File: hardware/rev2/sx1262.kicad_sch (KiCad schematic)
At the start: 36 parts, among them U2 SX1262IMLTRT, U3 PE4259, Y2 TCXO 32MHz

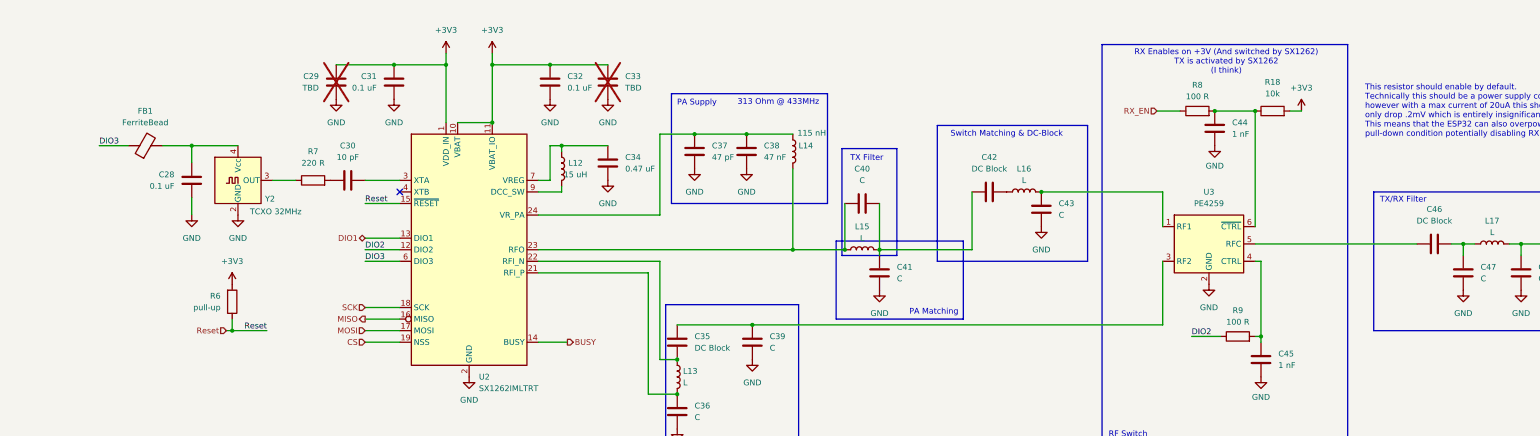
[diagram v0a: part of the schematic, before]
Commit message: set all applicable components for sx1262
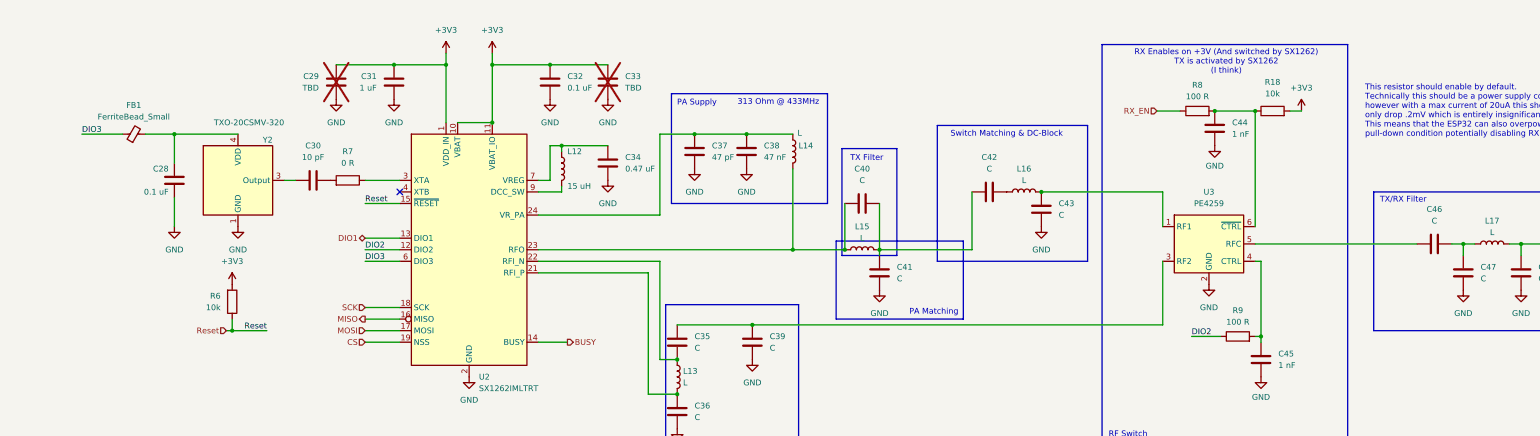
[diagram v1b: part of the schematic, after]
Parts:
- removed FB1: FerriteBead, symbol Device:FerriteBead
- removed Y2: TCXO 32MHz, symbol Oscillator:TCXO-14
- added FB1: FerriteBead_Small, Inductor_SMD:L_0402_1005Metric_Pad0.77x0.64mm_HandSolder, symbol Device:FerriteBead_Small
- added Y2: TXO-20CSMV-320, _footprints:TXO-20CSMV-320, symbol _symbols:TXO-20CSMV-320
- C28, C32: footprint Capacitor_SMD:C_0603_1608Metric_Pad1.08x0.95mm_HandSolder -> Capacitor_SMD:C_0402_1005Metric_Pad0.74x0.62mm_HandSolder; Mouser Part Number 81-GCJ188R71E104KA2D -> 81-GRM155R71H104KE4D
- C29, C33: footprint Capacitor_SMD:C_0603_1608Metric_Pad1.08x0.95mm_HandSolder -> Capacitor_SMD:C_0402_1005Metric_Pad0.74x0.62mm_HandSolder; now in the parts list
- C30: footprint Capacitor_SMD:C_0603_1608Metric_Pad1.08x0.95mm_HandSolder -> Capacitor_SMD:C_0402_1005Metric_Pad0.74x0.62mm_HandSolder; Mouser Part Number (none) -> 81-GJM1555C1H100JB01
- C31: value 0.1 uF -> 1 uF; footprint Capacitor_SMD:C_0603_1608Metric_Pad1.08x0.95mm_HandSolder -> Capacitor_SMD:C_0402_1005Metric_Pad0.74x0.62mm_HandSolder; Mouser Part Number 81-GCJ188R71E104KA2D -> 81-GRM155R61C105KA2D
- C34: footprint Capacitor_SMD:C_0603_1608Metric_Pad1.08x0.95mm_HandSolder -> Capacitor_SMD:C_0402_1005Metric_Pad0.74x0.62mm_HandSolder; Mouser Part Number (none) -> 81-GRM155R71A474KE1D
- C35, C42, C46: value DC Block -> C
- C37: Mouser Part Number (none) -> 81-GJM1555C1H470JB1D
- C38: Mouser Part Number (none) -> 81-GRM155R71C473KA01
- C44, C45: Mouser Part Number (none) -> 81-GRM155R72A102KA1D
- L12: Mouser Part Number (none) -> 810-MLZ1608N150LT000
- L14: value 115 nH -> L
- R18: footprint Inductor_SMD:L_0603_1608Metric_Pad1.05x0.95mm_HandSolder -> Resistor_SMD:R_0603_1608Metric_Pad0.98x0.95mm_HandSolder
- R6: value pull-up -> 10k; footprint Inductor_SMD:L_0603_1608Metric_Pad1.05x0.95mm_HandSolder -> Resistor_SMD:R_0603_1608Metric_Pad0.98x0.95mm_HandSolder
- R7: value 220 R -> 0 R; footprint Inductor_SMD:L_0603_1608Metric_Pad1.05x0.95mm_HandSolder -> Resistor_SMD:R_0402_1005Metric_Pad0.72x0.64mm_HandSolder; Mouser Part Number (none) -> 71-CRCW04020000Z0EDC
- R8, R9: footprint Inductor_SMD:L_0603_1608Metric_Pad1.05x0.95mm_HandSolder -> Resistor_SMD:R_0402_1005Metric_Pad0.72x0.64mm_HandSolder; Mouser Part Number (none) -> 71-CRCW0402-100
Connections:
- net DIO3: now also FB1.1
- net at U2.3 (XTA): now also R7.1; no longer C30.2
- net at C28.2: now also FB1.2, Y2.4 (VDD)
- net GND renamed 2
- net 2: now also Y2.1 (GND), Y2.GND (2)
- new net: C30.2, Y2.3 (Output)
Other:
- moved on the sheet: C28, C30, R7

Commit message: continued routing and layouting
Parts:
- renumbered C28 to C26, C30 to C27, C29 to C28, C31 to C29, C32 to C30, C33 to C31, C34 to C32, C35 to C33, C36 to C34, C37 to C35, C38 to C36, C39 to C37, C40 to C38, C41 to C39, C42 to C40, C43 to C41, C44 to C42, C45 to C43, C46 to C44, C47 to C45, C48 to C46, R6 to R17, R7 to R18, R8 to R19, R9 to R20, R18 to R21, U2 to U3, U3 to U4

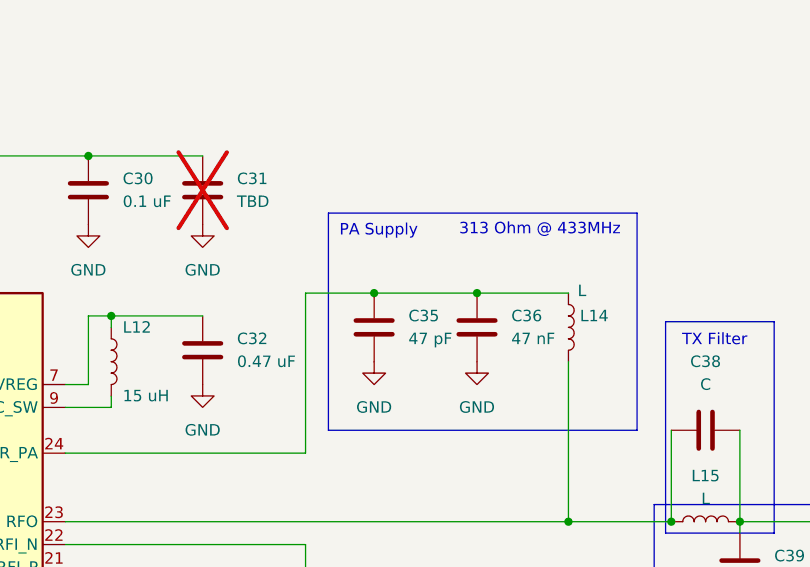
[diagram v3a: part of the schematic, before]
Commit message: continued layout, finished most of the RF stuff
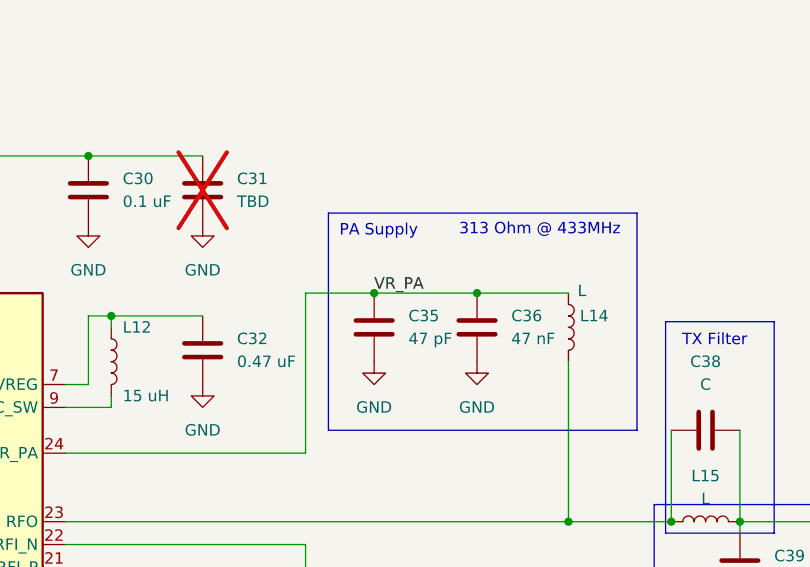
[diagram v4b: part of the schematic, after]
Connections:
- net VR_PA: now reaches C35.1, C36.1, L14.1, U3.24 (VR_PA)
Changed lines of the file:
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@@
+		)
+	)
+	(label "VR_PA"
+		(at 170.18 111.76 0)
+		(effects
+			(font
+				(size 1.27 1.27)
+			)
+			(justify left bottom)
 		)
 	)
@@
 		(length 1.27)
 		(shape round)
-		(at 181.61 111.76 0)
+		(at 238.76 124.46 0)
 		(fields_autoplaced yes)
 		(effects
@@
 			(justify left bottom)
 		)
-		(property "Net Class" "Power"
-			(at 182.3085 110.49 0)
+		(property "Net Class" "50 Ohm"
+			(at 239.4585 123.19 0)
 			(hide yes)
 			(show_name no)
@@
 		)
 		(property "Component Class" ""
-			(at -20.32 -24.13 0)
+			(at 69.85 -38.1 0)
 			(show_name no)
 			(do_not_autoplace no)

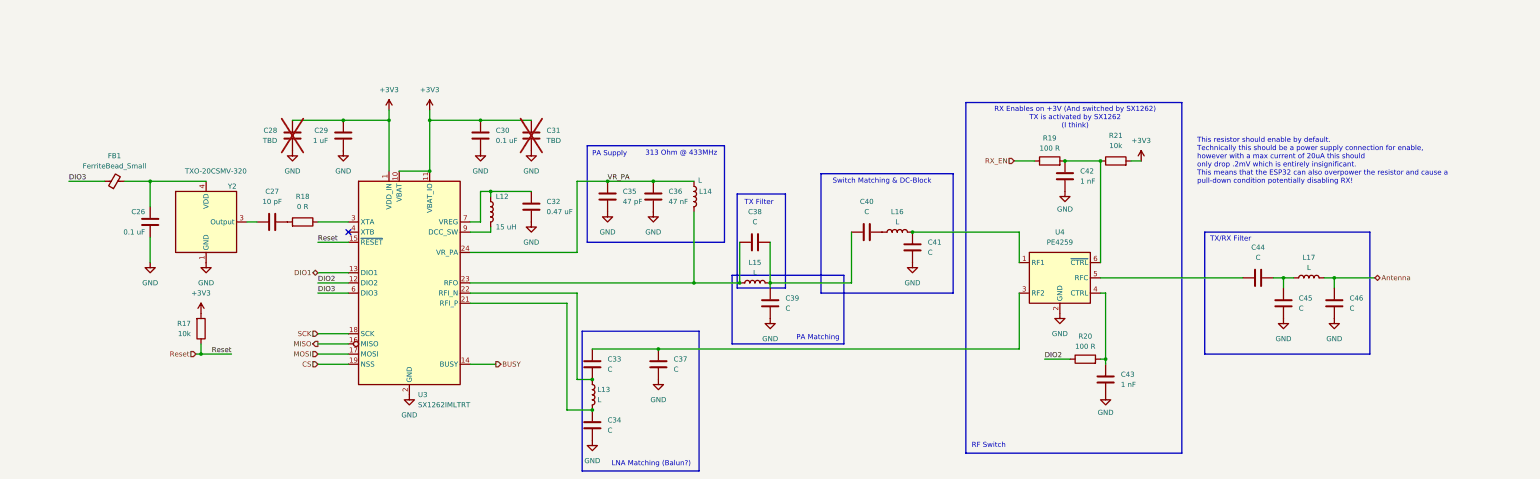
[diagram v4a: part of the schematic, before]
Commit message: finished routing most of the RF and power for SX1262 and ESP32, also decided final ish positions for both.
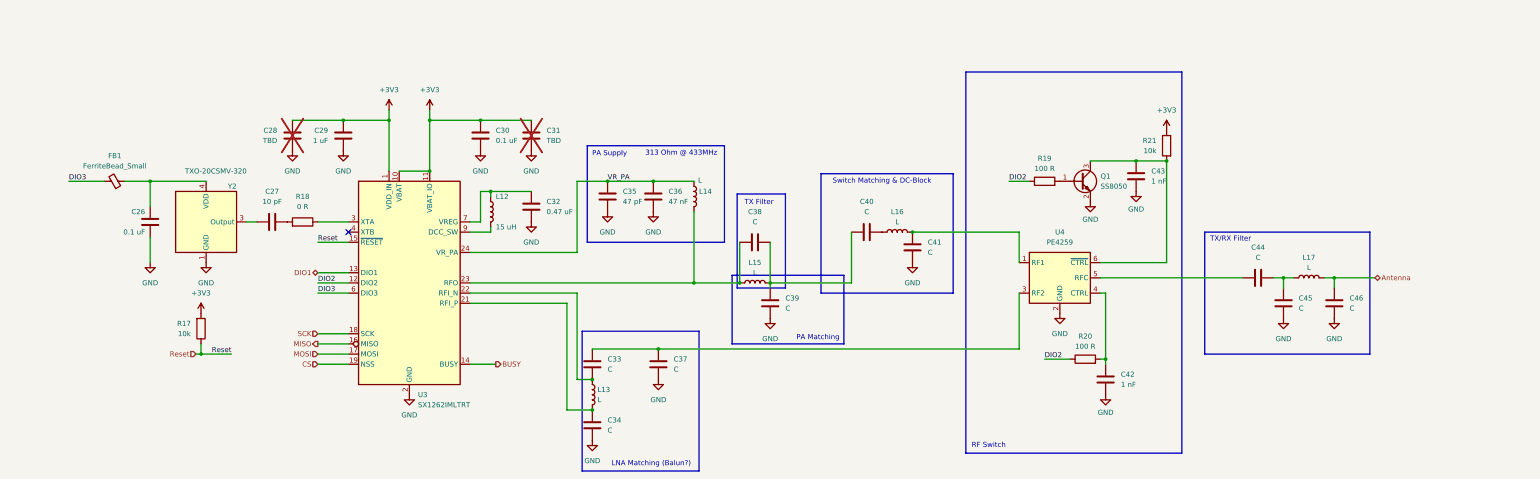
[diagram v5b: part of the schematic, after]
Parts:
- added Q1: SS8050, Package_TO_SOT_SMD:SOT-23, symbol Transistor_BJT:SS8050
- renumbered C43 to C42, C42 to C43
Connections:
- net RX_EN is gone; now on net DIO2: R19.1
- net +3V3: now also R21.1; no longer R21.2
- net DIO3: now also FB1.2; no longer FB1.1
- net at C43.1, U4.6 (~{CTRL}): now also R21.2, Q1.3 (C); no longer R19.2, R21.1
- net at C26.2, Y2.4 (VDD): now also FB1.1; no longer FB1.2
- net 2 renamed GND
- net GND: now also Y2.2 (GND), Q1.2 (E); no longer Y2.GND (2)
- new net: Q1.1 (B), R19.2
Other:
- note removed: "RX Enables on +3V (And switched by SX1262) TX is activated by SX1262 (I think)"
- note removed: "This resistor should enable by default. Technically this should be a power supply connection for enable, however with a max current of 20uA this should only drop .2mV which is entirely insignificant. This means that the ESP32 can also overpower the resistor and cause a pull-down condition potentially disabling RX!"
- moved on the sheet: C43, FB1, R19, R21

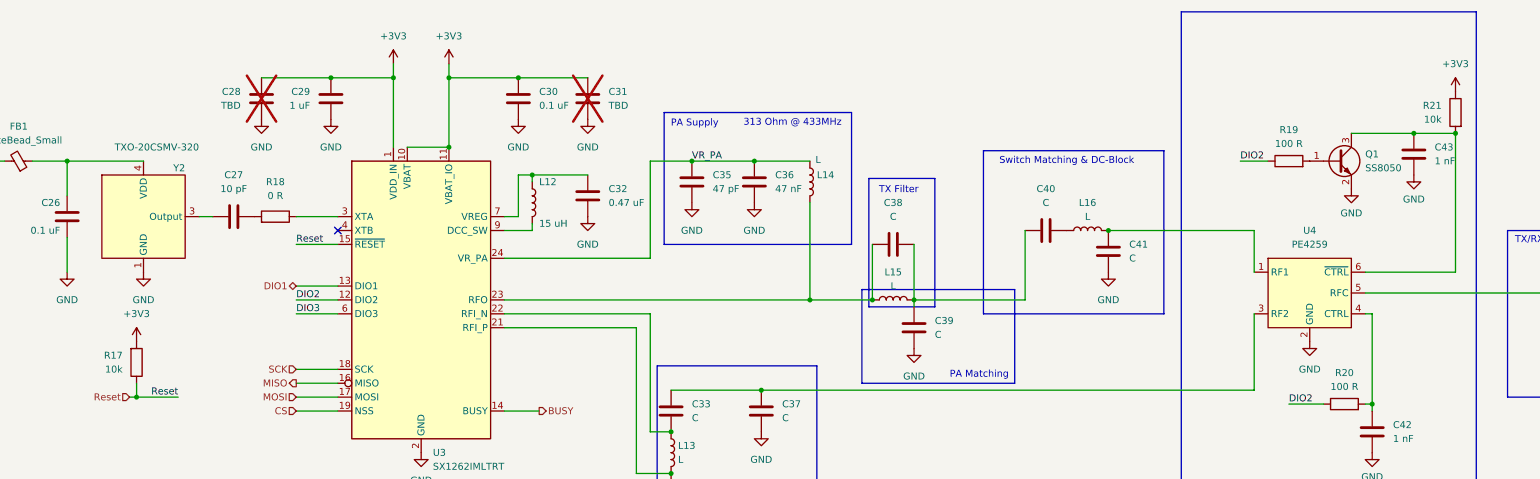
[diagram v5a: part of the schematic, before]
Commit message: routed everything ESP32 and SX1262, will hopefully work. still needs more testpoints
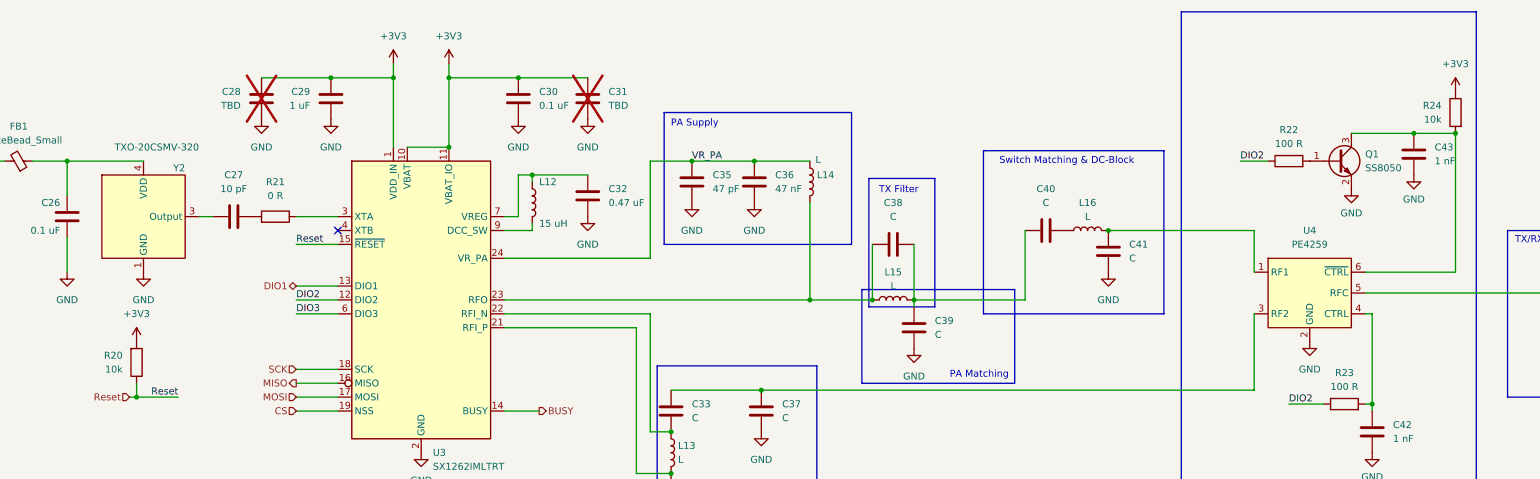
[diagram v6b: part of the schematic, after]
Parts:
- C26, C30: Mouser Part Number 81-GRM155R71H104KE4D -> 81-GRM155R71H104KE4D
- C29: Mouser Part Number 81-GRM155R61C105KA2D -> 81-GRM155R61C105KA2D
- C32: Mouser Part Number 81-GRM155R71A474KE1D -> 81-GRM155R71A474KE1D
- FB1: Mouser Part Number 81-BLM15PG100SN1D -> 81-BLM15PG100SN1D
- R21: renamed from R18; Mouser Part Number 71-CRCW04020000Z0EDC -> 71-CRCW04020000Z0EDC
- Y2: Mouser Part Number 520-TXO20CSMV320EYTR -> 520-TXO20CSMV320EYTR
- renumbered R17 to R20, R19 to R22, R20 to R23, R21 to R24
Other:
- note removed: "313 Ohm @ 433MHz"

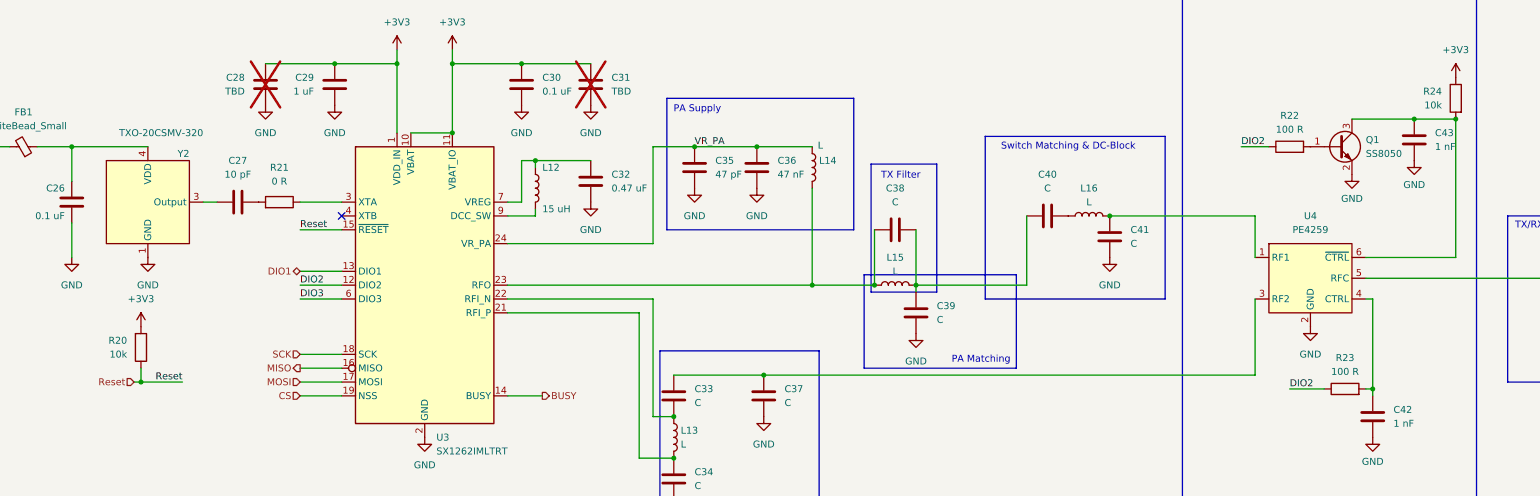
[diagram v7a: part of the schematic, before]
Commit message: added testpoints, added LEDs, fixed a lot of DRC stuff
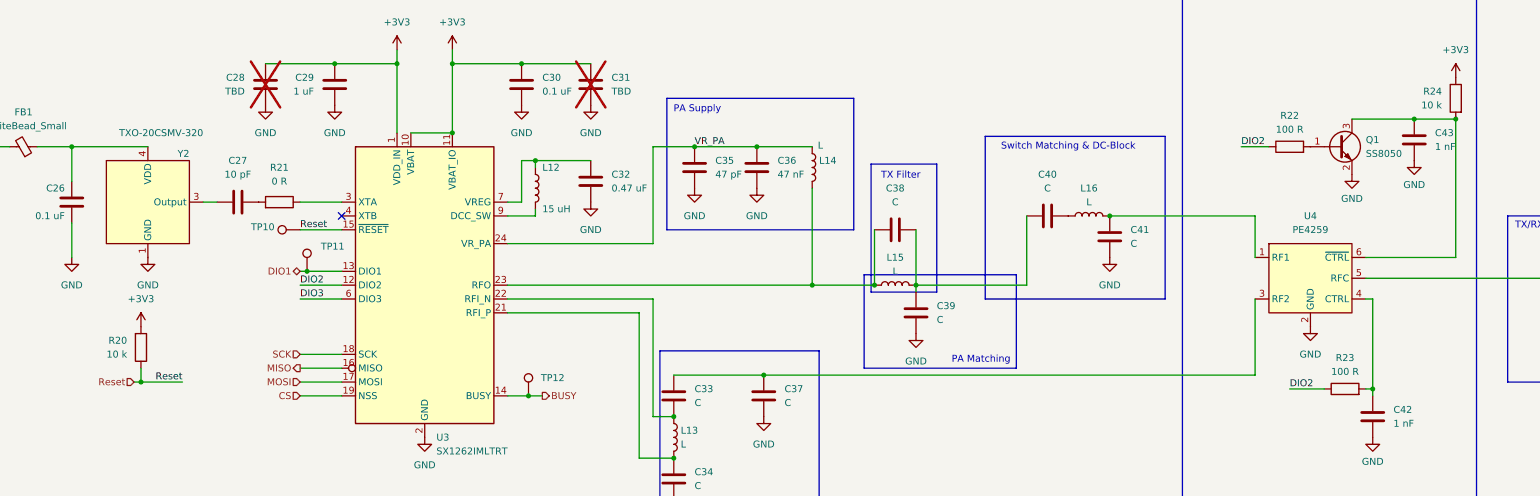
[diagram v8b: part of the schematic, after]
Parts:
- added TP10, TP11, TP12: TestPoint, TestPoint:TestPoint_Pad_D1.0mm, symbol Connector:TestPoint
- L12: Mouser Part Number 810-MLZ1608N150LT000 -> 810-MLZ1608N150LT000
- R20, R24: value 10k -> 10 k; Mouser Part Number (none) -> 71-CRCW060310K0JNEAC
- R21: Mouser Part Number 71-CRCW04020000Z0EDC -> 71-CRCW04020000Z0EDC
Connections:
- net BUSY: now also TP12.1
- net DIO1: now also TP11.1
- net Reset: now also TP10.1
